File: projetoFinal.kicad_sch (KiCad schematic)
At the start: 31 parts, among them J1 Conn_01x01_Male, J2 Conn_01x04, J3 Conn_01x01_Male, J4 Conn_01x01_Male, J5 Conn_01x01_Male, J6 Conn_01x04, U1 LM317_TO-220, U2 LM337_TO220

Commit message: roteamento feito
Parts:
- removed J2: Conn_01x04, Connector:FanPinHeader_1x04_P2.54mm_Vertical, symbol Connector_Generic:Conn_01x04
- added J2, J7: Conn_01x02, TerminalBlock_Phoenix:TerminalBlock_Phoenix_MKDS-1,5-2_1x02_P5.00mm_Horizontal, symbol Connector_Generic:Conn_01x02
- C1, C9: footprint Capacitor_THT:CP_Radial_Tantal_D6.0mm_P5.00mm -> Capacitor_THT:CP_Radial_D10.0mm_P2.50mm
- C10, C2, C4, C8: footprint Capacitor_THT:C_Axial_L3.8mm_D2.6mm_P7.50mm_Horizontal -> Capacitor_THT:C_Disc_D3.0mm_W2.0mm_P2.50mm
- C3, C7: footprint Capacitor_THT:C_Axial_L3.8mm_D2.6mm_P7.50mm_Horizontal -> Capacitor_THT:CP_Radial_D7.5mm_P2.50mm
- C5, C6: footprint Capacitor_THT:C_Axial_L3.8mm_D2.6mm_P7.50mm_Horizontal -> Capacitor_THT:CP_Radial_D5.0mm_P2.50mm
- D1, D2, D4, D5: footprint Diode_THT:D_A-405_P10.16mm_Horizontal -> Diode_THT:D_5W_P10.16mm_Horizontal
- HS1: footprint xHeatsink:Heatsink_AAVID_573300D00010G_TO-263 -> Heatsink:Heatsink_Stonecold_HS-132_32x14mm_2xFixation1.5mm
- J1, J3, J4, J5: footprint MountingHole:MountingHole_2.2mm_M2_DIN965_Pad -> footprints:Banana_Jack_1Pin
- J6: footprint Connector:FanPinHeader_1x04_P2.54mm_Vertical -> Connector_PinHeader_2.54mm:PinHeader_1x04_P2.54mm_Vertical
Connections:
- net GND: now also J2.1 (Pin_1), J7.2 (Pin_2)
- net at D3.2: now also J2.2 (Pin_2)
- net at D3.3: now also J7.1 (Pin_1)

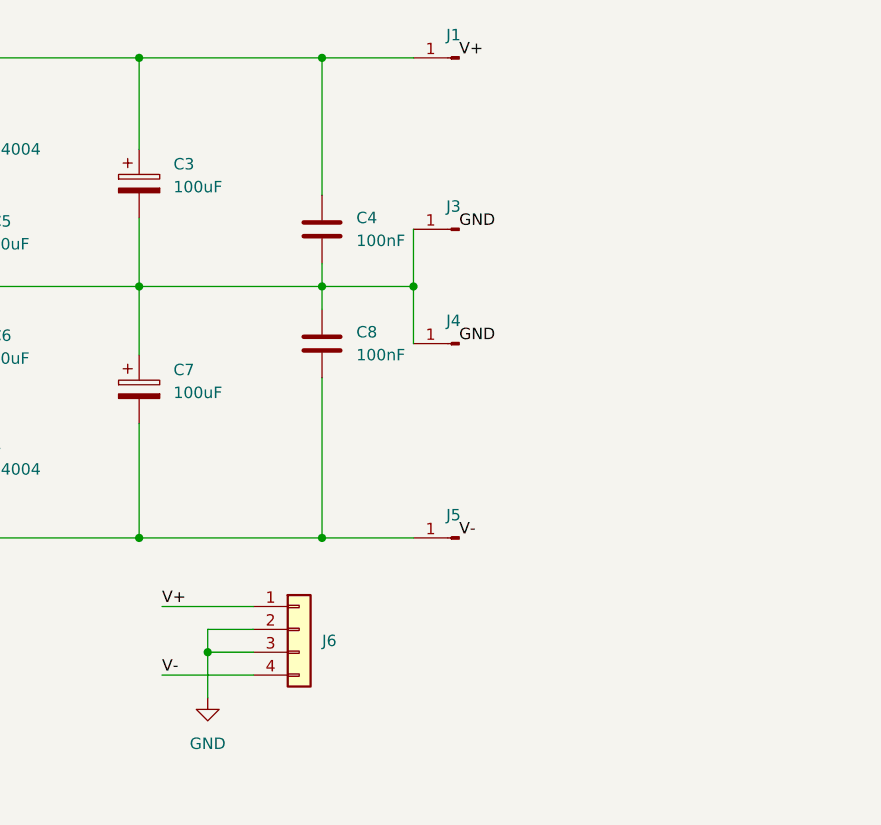
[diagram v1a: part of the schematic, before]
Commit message: novo roteamento da placa
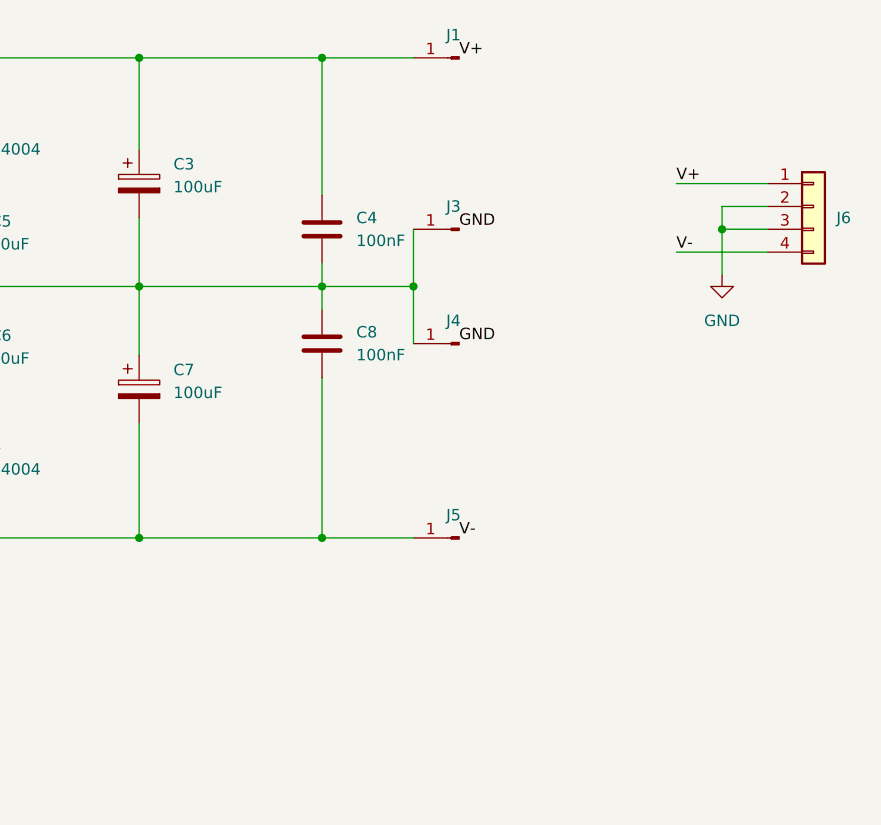
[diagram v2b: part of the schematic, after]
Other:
- moved on the sheet: J6
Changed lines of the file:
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@@
   (junction (at 165.1 71.12) (diameter 0) (color 0 0 0 0)
   )
-  (junction (at 193.04 137.16) (diameter 0) (color 0 0 0 0)
+  (junction (at 250.19 90.17) (diameter 0) (color 0 0 0 0)
   )
   (junction (at 148.59 96.52) (diameter 0) (color 0 0 0 0)
@@
     (stroke (width 0) (type default) (color 0 0 0 0))
   )
-  (wire (pts (xy 193.04 134.62) (xy 198.12 134.62))
+  (wire (pts (xy 250.19 87.63) (xy 255.27 87.63))
     (stroke (width 0) (type default) (color 0 0 0 0))
   )
@@
     (stroke (width 0) (type default) (color 0 0 0 0))
   )
-  (wire (pts (xy 193.04 137.16) (xy 198.12 137.16))
+  (wire (pts (xy 250.19 90.17) (xy 255.27 90.17))
     (stroke (width 0) (type default) (color 0 0 0 0))
   )
@@
     (stroke (width 0) (type default) (color 0 0 0 0))
   )
-  (wire (pts (xy 187.96 139.7) (xy 198.12 139.7))
+  (wire (pts (xy 245.11 92.71) (xy 255.27 92.71))
     (stroke (width 0) (type default) (color 0 0 0 0))
   )
@@
     (stroke (width 0) (type default) (color 0 0 0 0))
   )
-  (wire (pts (xy 193.04 137.16) (xy 193.04 134.62))
+  (wire (pts (xy 250.19 90.17) (xy 250.19 87.63))
     (stroke (width 0) (type default) (color 0 0 0 0))
   )
@@
     (stroke (width 0) (type default) (color 0 0 0 0))
   )
-  (wire (pts (xy 193.04 142.24) (xy 193.04 137.16))
+  (wire (pts (xy 250.19 95.25) (xy 250.19 90.17))
     (stroke (width 0) (type default) (color 0 0 0 0))
   )
@@
     (stroke (width 0) (type default) (color 0 0 0 0))
   )
-  (wire (pts (xy 187.96 132.08) (xy 198.12 132.08))
+  (wire (pts (xy 245.11 85.09) (xy 255.27 85.09))
     (stroke (width 0) (type default) (color 0 0 0 0))
   )
@@
     (effects (font (size 1.27 1.27)) (justify left bottom))
   )
-  (label "V-" (at 187.96 139.7 0)
+  (label "V-" (at 245.11 92.71 0)
     (effects (font (size 1.27 1.27)) (justify left bottom))
   )
@@
     (effects (font (size 1.27 1.27)) (justify left bottom))
   )
-  (label "V+" (at 187.96 132.08 0)
+  (label "V+" (at 245.11 85.09 0)
     (effects (font (size 1.27 1.27)) (justify left bottom))
   )
@@
     (pin "1")
   )
-  (symbol (lib_id "power:GND") (at 193.04 142.24 0) (unit 1)
-    (in_bom yes) (on_board yes) (fields_autoplaced)
-    (property "Reference" "#PWR0104" (id 0) (at 193.04 148.59 0)
-      (effects (font (size 1.27 1.27)) hide)
-    )
-    (property "Value" "GND" (id 1) (at 193.04 147.32 0))
-    (property "Footprint" "" (id 2) (at 193.04 142.24 0)
-      (effects (font (size 1.27 1.27)) hide)
-    )
-    (property "Datasheet" "" (id 3) (at 193.04 142.24 0)
+  (symbol (lib_id "power:GND") (at 250.19 95.25 0) (unit 1)
+    (in_bom yes) (on_board yes) (fields_autoplaced)
+    (property "Reference" "#PWR0104" (id 0) (at 250.19 101.6 0)
+      (effects (font (size 1.27 1.27)) hide)
+    )
+    (property "Value" "GND" (id 1) (at 250.19 100.33 0))
+    (property "Footprint" "" (id 2) (at 250.19 95.25 0)
+      (effects (font (size 1.27 1.27)) hide)
+    )
+    (property "Datasheet" "" (id 3) (at 250.19 95.25 0)
       (effects (font (size 1.27 1.27)) hide)
     )
@@
     (pin "2")
   )
-  (symbol (lib_id "Connector_Generic:Conn_01x04") (at 203.2 134.62 0) (unit 1)
-    (in_bom yes) (on_board yes) (fields_autoplaced)
-    (property "Reference" "J6" (id 0) (at 205.74 135.8899 0)
-      (effects (font (size 1.27 1.27)) (justify left))
-    )
-    (property "Value" "Conn_01x04" (id 1) (at 205.74 137.1599 0)
+  (symbol (lib_id "Connector_Generic:Conn_01x04") (at 260.35 87.63 0) (unit 1)
+    (in_bom yes) (on_board yes) (fields_autoplaced)
+    (property "Reference" "J6" (id 0) (at 262.89 88.8999 0)
+      (effects (font (size 1.27 1.27)) (justify left))
+    )
+    (property "Value" "Conn_01x04" (id 1) (at 262.89 90.1699 0)
       (effects (font (size 1.27 1.27)) (justify left) hide)
     )
-    (property "Footprint" "Connector_PinHeader_2.54mm:PinHeader_1x04_P2.54mm_Vertical" (id 2) (at 203.2 134.62 0)
-      (effects (font (size 1.27 1.27)) hide)
-    )
-    (property "Datasheet" "~" (id 3) (at 203.2 134.62 0)
-      (effects (font (size 1.27 1.27)) hide)
-    )
+    (property "Footprint" "Connector_PinHeader_2.54mm:PinHeader_1x04_P2.54mm_Vertical" (id 2) (at 260.35 87.63 0)
+      (effects (font (size 1.27 1.27)) hide)
+    )
+    (property "Datasheet" "~" (id 3) (at 260.35 87.63 0)
+      (effects (font (size 1.27 1.27)) hide)
+    )

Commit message: layout final
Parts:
- removed J1, J5: Conn_01x01_Male, footprints:Banana_Jack_1Pin, symbol Connector:Conn_01x01_Male
- C1, C9: footprint Capacitor_THT:CP_Radial_D10.0mm_P2.50mm -> Capacitor_THT:CP_Radial_D12.5mm_P5.00mm
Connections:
- net V+ is gone; now on an unnamed net: J6.1 (Pin_1)
- net V- is gone; now on an unnamed net: J6.4 (Pin_4)
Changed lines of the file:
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@@
-    (stroke (width 0) (type default) (color 0 0 0 0))
-  )
-  (wire (pts (xy 205.74 71.12) (xy 215.9 71.12))
     (stroke (width 0) (type default) (color 0 0 0 0))
   )
@@
     (stroke (width 0) (type default) (color 0 0 0 0))
   )
+  (wire (pts (xy 245.11 124.46) (xy 245.11 92.71))
+    (stroke (width 0) (type default) (color 0 0 0 0))
+  )
   (wire (pts (xy 157.48 71.12) (xy 157.48 59.69))
     (stroke (width 0) (type default) (color 0 0 0 0))
@@
     (stroke (width 0) (type default) (color 0 0 0 0))
   )
-  (wire (pts (xy 205.74 124.46) (xy 215.9 124.46))
+  (wire (pts (xy 205.74 124.46) (xy 245.11 124.46))
     (stroke (width 0) (type default) (color 0 0 0 0))
   )
@@
     (stroke (width 0) (type default) (color 0 0 0 0))
   )
+  (wire (pts (xy 245.11 71.12) (xy 245.11 85.09))
+    (stroke (width 0) (type default) (color 0 0 0 0))
+  )
   (wire (pts (xy 154.94 96.52) (xy 165.1 96.52))
     (stroke (width 0) (type default) (color 0 0 0 0))
@@
   )
   (wire (pts (xy 185.42 96.52) (xy 185.42 104.14))
+    (stroke (width 0) (type default) (color 0 0 0 0))
+  )
+  (wire (pts (xy 205.74 71.12) (xy 245.11 71.12))
     (stroke (width 0) (type default) (color 0 0 0 0))
   )
@@
   )
   (label "GND" (at 220.98 90.17 0)
-    (effects (font (size 1.27 1.27)) (justify left bottom))
-  )
-  (label "V+" (at 220.98 71.12 0)
-    (effects (font (size 1.27 1.27)) (justify left bottom))
-  )
-  (label "V-" (at 245.11 92.71 0)
-    (effects (font (size 1.27 1.27)) (justify left bottom))
-  )
-  (label "V-" (at 220.98 124.46 0)
-    (effects (font (size 1.27 1.27)) (justify left bottom))
-  )
-  (label "V+" (at 245.11 85.09 0)
     (effects (font (size 1.27 1.27)) (justify left bottom))
   )
@@
     (pin "1")
   )
-  (symbol (lib_id "Connector:Conn_01x01_Male") (at 220.98 124.46 180) (unit 1)
-    (in_bom yes) (on_board yes) (fields_autoplaced)
-    (property "Reference" "J5" (id 0) (at 220.345 121.92 0))
-    (property "Value" "Conn_01x01_Male" (id 1) (at 220.345 121.92 0)
-      (effects (font (size 1.27 1.27)) hide)
-    )
-    (property "Footprint" "footprints:Banana_Jack_1Pin" (id 2) (at 220.98 124.46 0)
-      (effects (font (size 1.27 1.27)) hide)
-    )
-    (property "Datasheet" "~" (id 3) (at 220.98 124.46 0)
+  (symbol (lib_id "power:GND") (at 220.98 90.17 0) (unit 1)
+    (in_bom yes) (on_board yes) (fields_autoplaced)
+    (property "Reference" "#PWR0105" (id 0) (at 220.98 96.52 0)
+      (effects (font (size 1.27 1.27)) hide)
+    )
+    (property "Value" "GND" (id 1) (at 220.98 95.25 0))
+    (property "Footprint" "" (id 2) (at 220.98 90.17 0)
+      (effects (font (size 1.27 1.27)) hide)
+    )
+    (property "Datasheet" "" (id 3) (at 220.98 90.17 0)
       (effects (font (size 1.27 1.27)) hide)
     )
@@
     (pin "1")
     (pin "2")
-  )
-  (symbol (lib_id "Connector:Conn_01x01_Male") (at 220.98 71.12 180) (unit 1)
-    (in_bom yes) (on_board yes) (fields_autoplaced)
-    (property "Reference" "J1" (id 0) (at 220.345 68.58 0))
-    (property "Value" "Conn_01x01_Male" (id 1) (at 220.345 68.58 0)
-      (effects (font (size 1.27 1.27)) hide)
-    )
-    (property "Footprint" "footprints:Banana_Jack_1Pin" (id 2) (at 220.98 71.12 0)
-      (effects (font (size 1.27 1.27)) hide)
-    )
-    (property "Datasheet" "~" (id 3) (at 220.98 71.12 0)
-      (effects (font (size 1.27 1.27)) hide)
-    )
-    (pin "1")
   )
   (symbol (lib_id "Device:C_Polarized") (at 185.42 85.09 0) (unit 1)
@@
       (effects (font (size 1.27 1.27)) (justify left))
     )
-    (property "Footprint" "Capacitor_THT:CP_Radial_D10.0mm_P2.50mm" (id 2) (at 111.4552 111.76 0)
+    (property "Footprint" "Capacitor_THT:CP_Radial_D12.5mm_P5.00mm" (id 2) (at 111.4552 111.76 0)
       (effects (font (size 1.27 1.27)) hide)
     )
@@
       (effects (font (size 1.27 1.27)) (justify left))
     )
-    (property "Footprint" "Capacitor_THT:CP_Radial_D10.0mm_P2.50mm" (id 2) (at 111.4552 88.9 0)
+    (property "Footprint" "Capacitor_THT:CP_Radial_D12.5mm_P5.00mm" (id 2) (at 111.4552 88.9 0)
       (effects (font (size 1.27 1.27)) hide)
     )
@@
     (pin "1")
     (pin "2")
+  )
+  (symbol (lib_id "power:GND") (at 220.98 102.87 0) (unit 1)
+    (in_bom yes) (on_board yes) (fields_autoplaced)
+    (property "Reference" "#PWR0106" (id 0) (at 220.98 109.22 0)
+      (effects (font (size 1.27 1.27)) hide)
+    )
+    (property "Value" "GND" (id 1) (at 220.98 107.95 0))
+    (property "Footprint" "" (id 2) (at 220.98 102.87 0)
+      (effects (font (size 1.27 1.27)) hide)
+    )
+    (property "Datasheet" "" (id 3) (at 220.98 102.87 0)
+      (effects (font (size 1.27 1.27)) hide)
+    )
+    (pin "1")
   )
   (symbol (lib_id "Regulator_Linear:LM317_TO-220") (at 148.59 71.12 0) (unit 1)
@@
       (reference "#PWR0104") (unit 1) (value "GND") (footprint "")
     )
+    (path "/2e5f41fc-2f19-44d1-b1fa-c41cca1163b8"
+      (reference "#PWR0105") (unit 1) (value "GND") (footprint "")
+    )
+    (path "/ce0cd4dd-b74d-4a32-a0de-fc215cb9ce71"
+      (reference "#PWR0106") (unit 1) (value "GND") (footprint "")
+    )
     (path "/a3a533eb-9712-4b1c-9794-2b1bbef5e0ff"
-      (reference "C1") (unit 1) (value "4700uF") (footprint "Capacitor_THT:CP_Radial_D10.0mm_P2.50mm")
+      (reference "C1") (unit 1) (value "4700uF") (footprint "Capacitor_THT:CP_Radial_D12.5mm_P5.00mm")
     )
     (path "/1ade4dff-4c0c-4a8d-a0a5-4714a29520b8"
@@
     )
     (path "/84bd8a6e-265c-493e-a929-a6e637651e39"
-      (reference "C9") (unit 1) (value "4700uF") (footprint "Capacitor_THT:CP_Radial_D10.0mm_P2.50mm")
+      (reference "C9") (unit 1) (value "4700uF") (footprint "Capacitor_THT:CP_Radial_D12.5mm_P5.00mm")
     )
     (path "/a6344f07-d3bf-43c5-bc47-4d2fb281ba23"
@@
       (reference "HS2") (unit 1) (value "Heatsink") (footprint "Heatsink:Heatsink_Stonecold_HS-132_32x14mm_2xFixation1.5mm")
     )
-    (path "/41cb776f-97db-4442-99b7-259c4cf7a394"
-      (reference "J1") (unit 1) (value "Conn_01x01_Male") (footprint "footprints:Banana_Jack_1Pin")
-    )
     (path "/27217235-23a6-43eb-b5e6-5d01546629e2"
       (reference "J2") (unit 1) (value "Conn_01x02") (footprint "TerminalBlock_Phoenix:TerminalBlock_Phoenix_MKDS-1,5-2_1x02_P5.00mm_Horizontal")
@@
       (reference "J4") (unit 1) (value "Conn_01x01_Male") (footprint "footprints:Banana_Jack_1Pin")
     )
-    (path "/30e41159-5267-46e6-8d9c-1174e7b44836"
-      (reference "J5") (unit 1) (value "Conn_01x01_Male") (footprint "footprints:Banana_Jack_1Pin")
-    )
     (path "/57f31529-1499-458f-9a48-eb59bb575b06"
